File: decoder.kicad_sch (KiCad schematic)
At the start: 15 parts

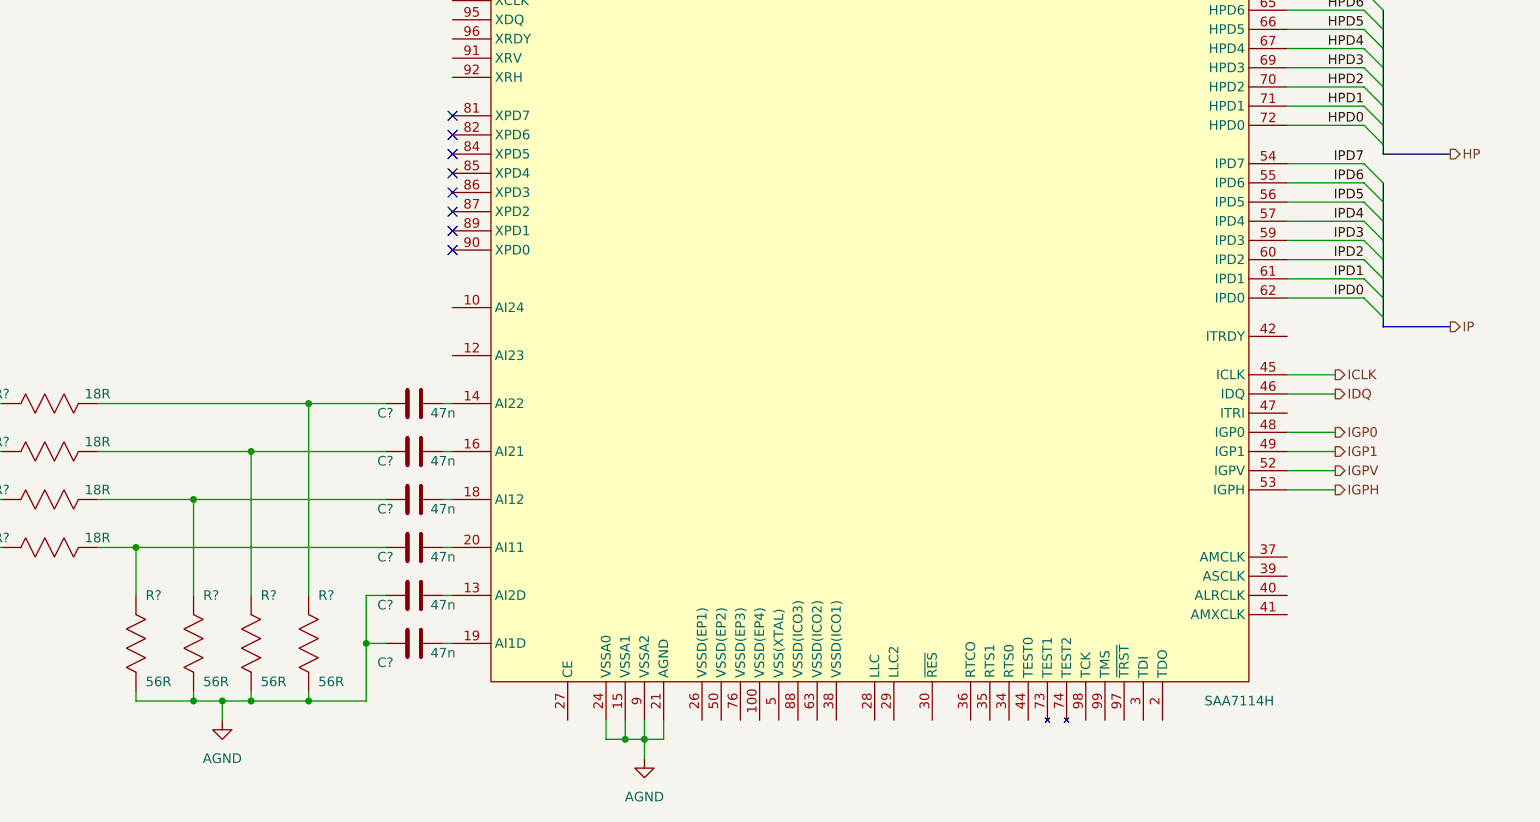
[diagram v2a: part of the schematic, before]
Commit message: added buses, title block info
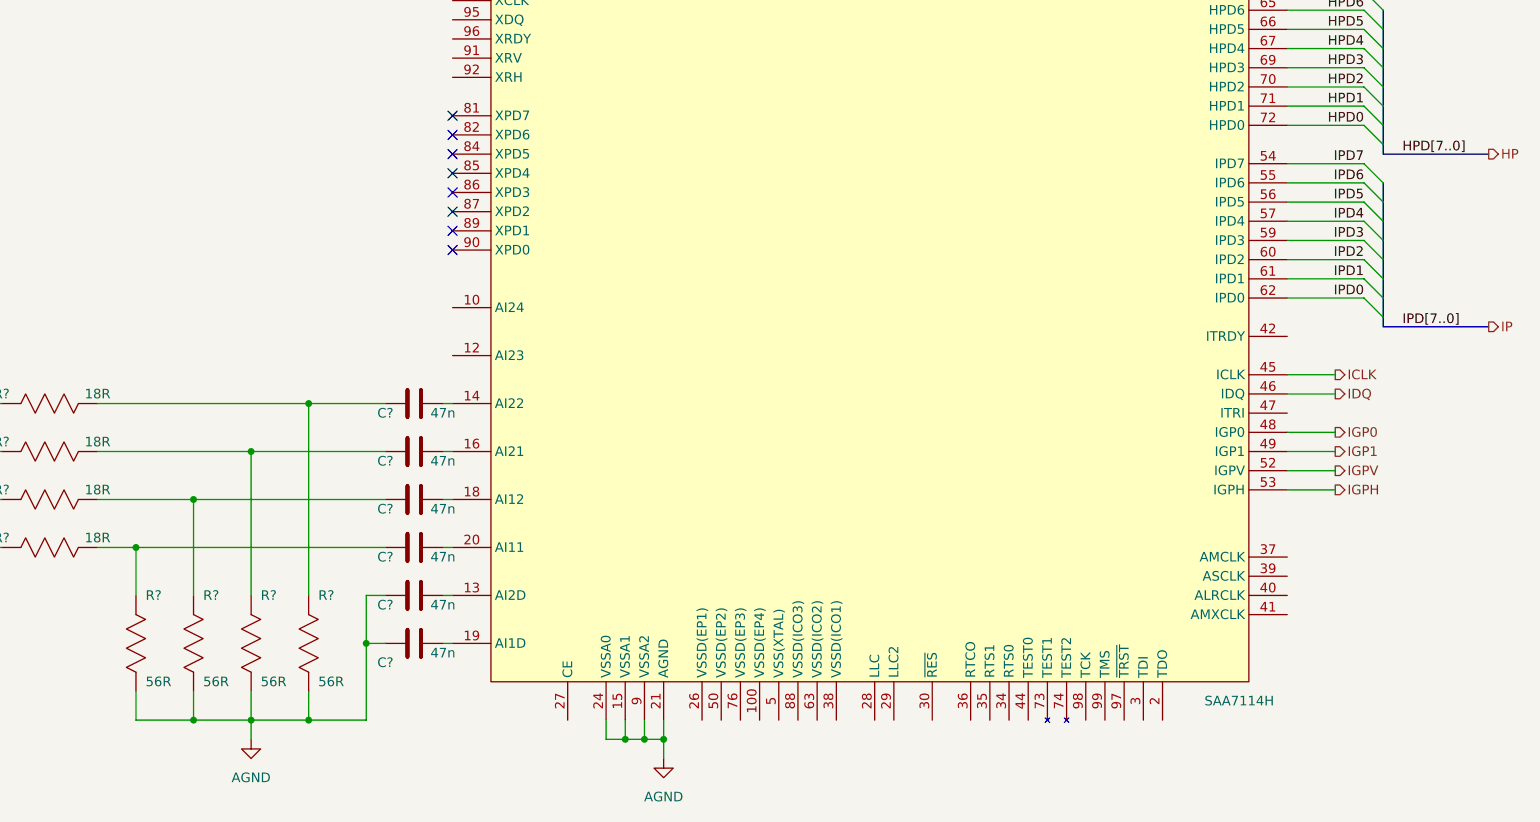
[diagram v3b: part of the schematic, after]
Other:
- title: (none) -> Time Base Corrector and Video Scaler
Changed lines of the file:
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@@
 (kicad_sch (version 20230121) (generator eeschema)
   (paper "A4")
+  (title_block
+    (title "Time Base Corrector and Video Scaler")
+    (date "2024-01-15")
+    (rev "1")
+  )
   (junction (at 71.12 121.92) (diameter 0) (color 0 0 0 0)
   )
-  (junction (at 78.74 148.59) (diameter 0) (color 0 0 0 0)
-  )
-  (junction (at 74.93 148.59) (diameter 0) (color 0 0 0 0)
+  (junction (at 78.74 151.13) (diameter 0) (color 0 0 0 0)
   )
   (junction (at 93.98 140.97) (diameter 0) (color 0 0 0 0)
@@
   (junction (at 63.5 128.27) (diameter 0) (color 0 0 0 0)
   )
+  (junction (at 133.35 153.67) (diameter 0) (color 0 0 0 0)
+  )
   (junction (at 130.81 153.67) (diameter 0) (color 0 0 0 0)
   )
-  (junction (at 71.12 148.59) (diameter 0) (color 0 0 0 0)
-  )
-  (junction (at 86.36 148.59) (diameter 0) (color 0 0 0 0)
+  (junction (at 71.12 151.13) (diameter 0) (color 0 0 0 0)
+  )
+  (junction (at 86.36 151.13) (diameter 0) (color 0 0 0 0)
   )
   (junction (at 78.74 115.57) (diameter 0) (color 0 0 0 0)
@@
     (stroke (width 0) (type default))
   )
+  (bus (pts (xy 228.6 97.79) (xy 228.6 99.06))
+    (stroke (width 0) (type default))
+  )
   (bus (pts (xy 228.6 95.25) (xy 228.6 97.79))
     (stroke (width 0) (type default))
@@
     (stroke (width 0) (type default))
   )
-  (wire (pts (xy 93.98 140.97) (xy 93.98 148.59))
+  (wire (pts (xy 93.98 140.97) (xy 93.98 151.13))
     (stroke (width 0) (type default))
   )
@@
     (stroke (width 0) (type default))
   )
-  (bus (pts (xy 228.6 76.2) (xy 237.49 76.2))
+  (bus (pts (xy 228.6 76.2) (xy 242.57 76.2))
     (stroke (width 0) (type default))
   )
@@
     (stroke (width 0) (type default))
   )
-  (wire (pts (xy 74.93 148.59) (xy 74.93 151.13))
+  (wire (pts (xy 78.74 151.13) (xy 78.74 153.67))
     (stroke (width 0) (type default))
   )
@@
     (stroke (width 0) (type default))
   )
-  (wire (pts (xy 71.12 148.59) (xy 74.93 148.59))
-    (stroke (width 0) (type default))
-  )
   (bus (pts (xy 228.6 57.15) (xy 228.6 59.69))
     (stroke (width 0) (type default))
@@
     (stroke (width 0) (type default))
   )
-  (wire (pts (xy 86.36 147.32) (xy 86.36 148.59))
-    (stroke (width 0) (type default))
-  )
-  (wire (pts (xy 78.74 148.59) (xy 86.36 148.59))
+  (wire (pts (xy 71.12 151.13) (xy 78.74 151.13))
+    (stroke (width 0) (type default))
+  )
+  (wire (pts (xy 86.36 147.32) (xy 86.36 151.13))
+    (stroke (width 0) (type default))
+  )
+  (wire (pts (xy 78.74 151.13) (xy 86.36 151.13))
     (stroke (width 0) (type default))
   )
@@
     (stroke (width 0) (type default))
   )
-  (wire (pts (xy 78.74 148.59) (xy 74.93 148.59))
-    (stroke (width 0) (type default))
-  )
   (bus (pts (xy 228.6 92.71) (xy 228.6 95.25))
     (stroke (width 0) (type default))
   )
-  (bus (pts (xy 228.6 99.06) (xy 237.49 99.06))
-    (stroke (width 0) (type default))
-  )
   (wire (pts (xy 215.9 105.41) (xy 222.25 105.41))
     (stroke (width 0) (type default))
@@
     (stroke (width 0) (type default))
   )
+  (bus (pts (xy 228.6 99.06) (xy 242.57 99.06))
+    (stroke (width 0) (type default))
+  )
   (wire (pts (xy 78.74 115.57) (xy 78.74 134.62))
     (stroke (width 0) (type default))
@@
     (stroke (width 0) (type default))
   )
-  (wire (pts (xy 63.5 148.59) (xy 71.12 148.59))
+  (wire (pts (xy 63.5 151.13) (xy 71.12 151.13))
     (stroke (width 0) (type default))
   )
@@
     (stroke (width 0) (type default))
   )
-  (wire (pts (xy 71.12 147.32) (xy 71.12 148.59))
+  (wire (pts (xy 71.12 147.32) (xy 71.12 151.13))
     (stroke (width 0) (type default))
   )
@@
     (stroke (width 0) (type default))
   )
-  (wire (pts (xy 130.81 153.67) (xy 130.81 156.21))
+  (wire (pts (xy 133.35 153.67) (xy 133.35 156.21))
     (stroke (width 0) (type default))
   )
@@
     (stroke (width 0) (type default))
   )
+  (wire (pts (xy 215.9 95.25) (xy 226.06 95.25))
+    (stroke (width 0) (type default))
+  )
+  (wire (pts (xy 63.5 147.32) (xy 63.5 151.13))
+    (stroke (width 0) (type default))
+  )
   (bus (pts (xy 228.6 64.77) (xy 228.6 67.31))
     (stroke (width 0) (type default))
   )
-  (bus (pts (xy 228.6 97.79) (xy 228.6 99.06))
-    (stroke (width 0) (type default))
-  )
   (wire (pts (xy 104.14 109.22) (xy 105.41 109.22))
     (stroke (width 0) (type default))
@@
     (stroke (width 0) (type default))
   )
-  (wire (pts (xy 63.5 148.59) (xy 63.5 147.32))
-    (stroke (width 0) (type default))
-  )
   (wire (pts (xy 93.98 134.62) (xy 93.98 140.97))
     (stroke (width 0) (type default))
@@
     (stroke (width 0) (type default))
   )
-  (wire (pts (xy 93.98 148.59) (xy 86.36 148.59))
+  (wire (pts (xy 93.98 151.13) (xy 86.36 151.13))
     (stroke (width 0) (type default))
   )
@@
     (stroke (width 0) (type default))
   )
-  (wire (pts (xy 215.9 95.25) (xy 226.06 95.25))
-    (stroke (width 0) (type default))
-  )
   (wire (pts (xy 78.74 115.57) (xy 96.52 115.57))
     (stroke (width 0) (type default))
@@
     (stroke (width 0) (type default))
   )
-  (wire (pts (xy 78.74 147.32) (xy 78.74 148.59))
+  (wire (pts (xy 78.74 147.32) (xy 78.74 151.13))
     (stroke (width 0) (type default))
   )
@@
     (effects (font (size 1.27 1.27)) (justify right bottom))
   )
+  (label "HPD[7..0]" (at 231.14 76.2 0) (fields_autoplaced)
+    (effects (font (size 1.27 1.27)) (justify left bottom))
+  )
   (label "HPD2" (at 226.06 67.31 180) (fields_autoplaced)
     (effects (font (size 1.27 1.27)) (justify right bottom))
+  )
+  (label "IPD[7..0]" (at 231.14 99.06 0) (fields_autoplaced)
+    (effects (font (size 1.27 1.27)) (justify left bottom))
   )
   (label "IPD4" (at 226.06 85.09 180) (fields_autoplaced)
@@
     (effects (font (size 1.27 1.27)) (justify left))
   )
-  (hierarchical_label "IP" (shape output) (at 237.49 99.06 0) (fields_autoplaced)
+  (hierarchical_label "IP" (shape output) (at 242.57 99.06 0) (fields_autoplaced)
     (effects (font (size 1.27 1.27)) (justify left))
   )
@@
     (effects (font (size 1.27 1.27)) (justify right))
   )
-  (hierarchical_label "HP" (shape output) (at 237.49 76.2 0) (fields_autoplaced)
+  (hierarchical_label "HP" (shape output) (at 242.57 76.2 0) (fields_autoplaced)
     (effects (font (size 1.27 1.27)) (justify left))
   )
@@
     )
   )
-  (symbol (lib_id "tbc:AGND") (at 130.81 156.21 0) (unit 1)
+  (symbol (lib_id "tbc:AGND") (at 133.35 156.21 0) (unit 1)
     (in_bom yes) (on_board yes) (dnp no) (fields_autoplaced)
-    (property "Reference" "#PWR02" (at 130.81 162.56 0)
-      (effects (font (size 1.27 1.27)) hide)
-    )
-    (property "Value" "AGND" (at 130.81 161.29 0)
-      (effects (font (size 1.27 1.27)))
-    )
-    (property "Footprint" "" (at 130.81 156.21 0)
-      (effects (font (size 1.27 1.27)) hide)
-    )
-    (property "Datasheet" "" (at 130.81 156.21 0)
+    (property "Reference" "#PWR02" (at 133.35 162.56 0)
+      (effects (font (size 1.27 1.27)) hide)
+    )
+    (property "Value" "AGND" (at 133.35 161.29 0)
+      (effects (font (size 1.27 1.27)))
+    )
+    (property "Footprint" "" (at 133.35 156.21 0)
+      (effects (font (size 1.27 1.27)) hide)
+    )
+    (property "Datasheet" "" (at 133.35 156.21 0)
       (effects (font (size 1.27 1.27)) hide)
     )
@@
     )
   )
-  (symbol (lib_id "tbc:AGND") (at 74.93 151.13 0) (unit 1)
+  (symbol (lib_id "tbc:AGND") (at 78.74 153.67 0) (unit 1)
     (in_bom yes) (on_board yes) (dnp no) (fields_autoplaced)
-    (property "Reference" "#PWR01" (at 74.93 157.48 0)
-      (effects (font (size 1.27 1.27)) hide)
-    )
-    (property "Value" "AGND" (at 74.93 156.21 0)
-      (effects (font (size 1.27 1.27)))
-    )
-    (property "Footprint" "" (at 74.93 151.13 0)
-      (effects (font (size 1.27 1.27)) hide)
-    )
-    (property "Datasheet" "" (at 74.93 151.13 0)
-      (effects (font (size 1.27 1.27)) hide)
-    )
+    (property "Reference" "#PWR01" (at 78.74 160.02 0)
+      (effects (font (size 1.27 1.27)) hide)
+    )
+    (property "Value" "AGND" (at 78.74 158.75 0)
+      (effects (font (size 1.27 1.27)))
+    )
+    (property "Footprint" "" (at 78.74 153.67 0)
+      (effects (font (size 1.27 1.27)) hide)
+    )
+    (property "Datasheet" "" (at 78.74 153.67 0)
+      (effects (font (size 1.27 1.27)) hide)
+    )

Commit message: added frame memory symbol and updated schematic
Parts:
- C? (x6): MPN GCJ188R71E473KA01D -> (none)
- R? (x4): MPN RC0603FR-0718RL -> (none)
- R? (x4): MPN RC0603FR-0756RL -> (none)
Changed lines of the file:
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@@
-      (effects (font (size 1.27 1.27)) (justify left) hide)
-    )
-    (property "MPN" "GCJ188R71E473KA01D" (at 86.36 129.54 0) (show_name)
       (effects (font (size 1.27 1.27)) (justify left) hide)
     )
@@
     )
     (property "Datasheet" "https://www.yageo.com/upload/media/product/products/datasheet/rchip/PYu-RC_Group_51_RoHS_L_12.pdf" (at 35.56 134.62 0) (show_name)
-      (effects (font (size 1.27 1.27)) (justify left) hide)
-    )
-    (property "MPN" "RC0603FR-0718RL" (at 35.56 129.54 0) (show_name)
       (effects (font (size 1.27 1.27)) (justify left) hide)
     )
@@
       (effects (font (size 1.27 1.27)) (justify right))
     )
-    (property "Value" "56R" (at 64.77 146.05 90)
-      (effects (font (size 1.27 1.27)) (justify right))
+    (property "Value" "56R" (at 64.77 146.05 0)
+      (effects (font (size 1.27 1.27)))
     )
     (property "Footprint" "" (at 71.12 157.48 0)
@@
     )
     (property "Datasheet" "https://www.yageo.com/upload/media/product/products/datasheet/rchip/PYu-RC_Group_51_RoHS_L_12.pdf" (at 76.2 157.48 0) (show_name)
-      (effects (font (size 1.27 1.27)) (justify left) hide)
-    )
-    (property "MPN" "RC0603FR-0756RL" (at 71.12 157.48 0) (show_name)
       (effects (font (size 1.27 1.27)) (justify left) hide)
     )
@@
       (effects (font (size 1.27 1.27)) (justify right))
     )
-    (property "Value" "56R" (at 80.01 146.05 90)
-      (effects (font (size 1.27 1.27)) (justify right))
+    (property "Value" "56R" (at 80.01 146.05 0)
+      (effects (font (size 1.27 1.27)))
     )
     (property "Footprint" "" (at 86.36 157.48 0)
@@
     )
     (property "Datasheet" "https://www.yageo.com/upload/media/product/products/datasheet/rchip/PYu-RC_Group_51_RoHS_L_12.pdf" (at 91.44 157.48 0) (show_name)
-      (effects (font (size 1.27 1.27)) (justify left) hide)
-    )
-    (property "MPN" "RC0603FR-0756RL" (at 86.36 157.48 0) (show_name)
       (effects (font (size 1.27 1.27)) (justify left) hide)
     )
@@
       (effects (font (size 1.27 1.27)) (justify left) hide)
     )
-    (property "MPN" "GCJ188R71E473KA01D" (at 86.36 123.19 0) (show_name)
-      (effects (font (size 1.27 1.27)) (justify left) hide)
-    )
     (property "Mouser" "81-GCJ188R71E473KA1D" (at 86.36 125.73 0) (show_name)
       (effects (font (size 1.27 1.27)) (justify left) hide)
@@
     )
     (property "Datasheet" "https://au.mouser.com/datasheet/2/281/1/GCJ188R71E473KA01_02B-3140701.pdf" (at 86.36 140.97 0) (show_name)
-      (effects (font (size 1.27 1.27)) (justify left) hide)
-    )
-    (property "MPN" "GCJ188R71E473KA01D" (at 86.36 135.89 0) (show_name)
       (effects (font (size 1.27 1.27)) (justify left) hide)
     )
@@
       (effects (font (size 1.27 1.27)) (justify right))
     )
-    (property "Value" "56R" (at 72.39 146.05 90)
-      (effects (font (size 1.27 1.27)) (justify right))
+    (property "Value" "56R" (at 72.39 146.05 0)
+      (effects (font (size 1.27 1.27)))
     )
     (property "Footprint" "" (at 78.74 157.48 0)
@@
       (effects (font (size 1.27 1.27)) (justify left) hide)
     )
-    (property "MPN" "RC0603FR-0756RL" (at 78.74 157.48 0) (show_name)
-      (effects (font (size 1.27 1.27)) (justify left) hide)
-    )
     (property "Mouser" " 603-RC0603FR-0756RL " (at 81.28 157.48 0) (show_name)
       (effects (font (size 1.27 1.27)) (justify left) hide)
@@
     )
     (property "Datasheet" "https://www.yageo.com/upload/media/product/products/datasheet/rchip/PYu-RC_Group_51_RoHS_L_12.pdf" (at 35.56 121.92 0) (show_name)
-      (effects (font (size 1.27 1.27)) (justify left) hide)
-    )
-    (property "MPN" "RC0603FR-0718RL" (at 35.56 116.84 0) (show_name)
       (effects (font (size 1.27 1.27)) (justify left) hide)
     )
@@
       (effects (font (size 1.27 1.27)) (justify left) hide)
     )
-    (property "MPN" "GCJ188R71E473KA01D" (at 86.36 116.84 0) (show_name)
-      (effects (font (size 1.27 1.27)) (justify left) hide)
-    )
     (property "Mouser" "81-GCJ188R71E473KA1D" (at 86.36 119.38 0) (show_name)
       (effects (font (size 1.27 1.27)) (justify left) hide)
@@
       (effects (font (size 1.27 1.27)) (justify left) hide)
     )
-    (property "MPN" "RC0603FR-0718RL" (at 35.56 123.19 0) (show_name)
-      (effects (font (size 1.27 1.27)) (justify left) hide)
-    )
     (property "Mouser" "603-RC0603FR-0718RL" (at 35.56 125.73 0) (show_name)
       (effects (font (size 1.27 1.27)) (justify left) hide)
@@
       (effects (font (size 1.27 1.27)) (justify left) hide)
     )
-    (property "MPN" "GCJ188R71E473KA01D" (at 86.36 142.24 0) (show_name)
-      (effects (font (size 1.27 1.27)) (justify left) hide)
-    )
     (property "Mouser" "81-GCJ188R71E473KA1D" (at 86.36 144.78 0) (show_name)
       (effects (font (size 1.27 1.27)) (justify left) hide)
@@
     )
     (property "Datasheet" "https://au.mouser.com/datasheet/2/281/1/GCJ188R71E473KA01_02B-3140701.pdf" (at 86.36 153.67 0) (show_name)
-      (effects (font (size 1.27 1.27)) (justify left) hide)
-    )
-    (property "MPN" "GCJ188R71E473KA01D" (at 86.36 148.59 0) (show_name)
       (effects (font (size 1.27 1.27)) (justify left) hide)
     )
@@
       (effects (font (size 1.27 1.27)) (justify right))
     )
-    (property "Value" "56R" (at 87.63 146.05 90)
-      (effects (font (size 1.27 1.27)) (justify right))
+    (property "Value" "56R" (at 87.63 146.05 0)
+      (effects (font (size 1.27 1.27)))
     )
     (property "Footprint" "" (at 93.98 157.48 0)
@@
       (effects (font (size 1.27 1.27)) (justify left) hide)
     )
-    (property "MPN" "RC0603FR-0756RL" (at 93.98 157.48 0) (show_name)
-      (effects (font (size 1.27 1.27)) (justify left) hide)
-    )
     (property "Mouser" " 603-RC0603FR-0756RL " (at 96.52 157.48 0) (show_name)
       (effects (font (size 1.27 1.27)) (justify left) hide)
@@
       (effects (font (size 1.27 1.27)) (justify left) hide)
     )
-    (property "MPN" "RC0603FR-0718RL" (at 35.56 135.89 0) (show_name)
-      (effects (font (size 1.27 1.27)) (justify left) hide)
-    )

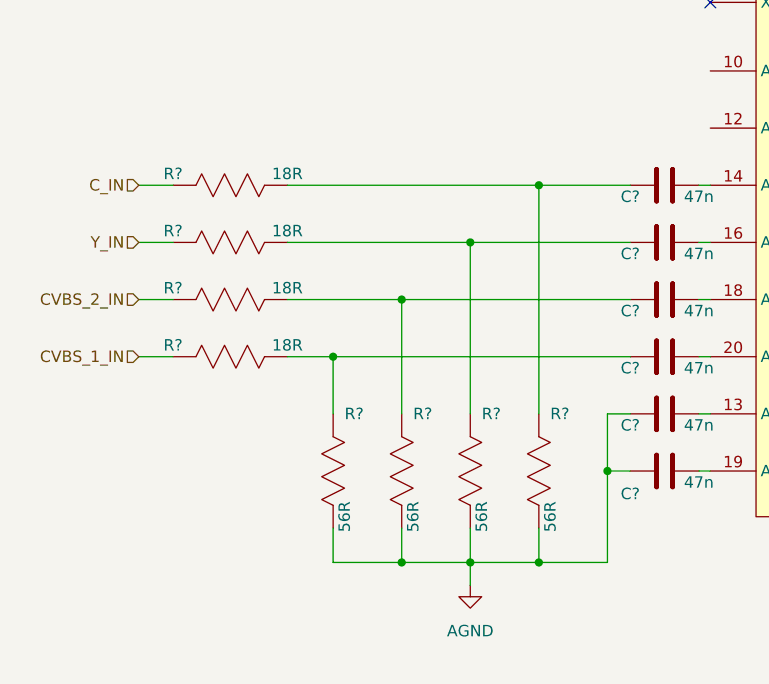
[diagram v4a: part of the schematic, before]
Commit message: continued on schematic, added power sheet
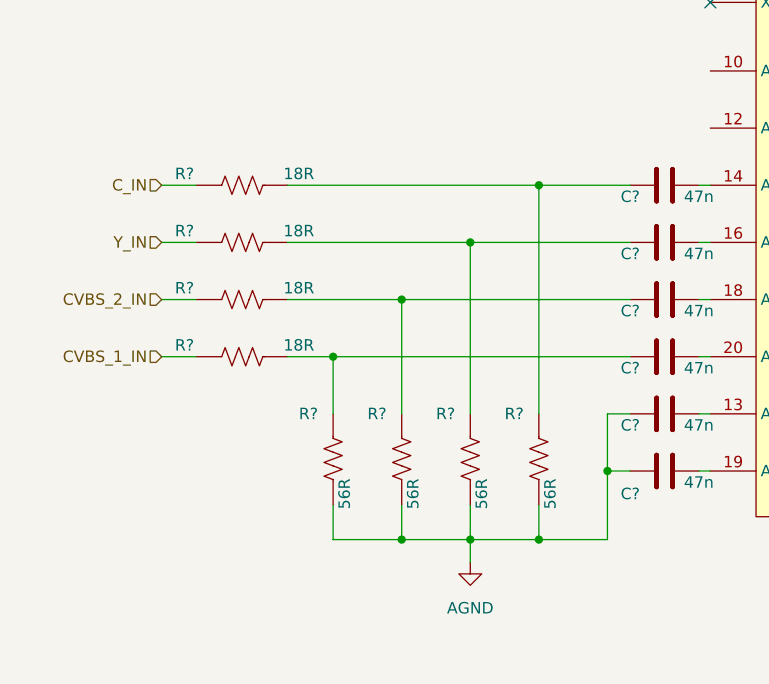
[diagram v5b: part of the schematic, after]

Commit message: updates to power, ferrites etc
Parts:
- added C?: 22u|25V, symbol tbc:GRM32ER71E226KE15L
- added C? (x13): 100n, symbol tbc:GCJ188R71H104KA12D
- added L?: 10uH, symbol tbc:DFE201610E-100M=P2
- R? (x4): value 18R -> 18
- R? (x4): value 56R -> 56
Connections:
- net AGND is gone; now on net GND: C?.1, C?.1, R?.1, R?.1, R?.1, R?.1, U?.15 (VSSA1), U?.21 (AGND), U?.24 (VSSA0), U?.9 (VSSA2)
- net +3V3: now reaches U?.1 (VDDD(EP1))
- net +3V3: now also U?.25 (VDDD(EP2)), U?.33 (VDDD(ICO1)), U?.43 (VDDD(ICO2)), U?.51 (VDDD(EP3)), U?.58 (VDDD(ICO3)), U?.68 (VDDD(ICO4)), U?.75 (VDDD(EP4)), U?.83 (VDDD(ICO5)), U?.93 (VDDD(ICO6)), C?.2, C?.2, C?.2, C?.2, C?.2, C?.2, C?.2, C?.2, C?.2, C?.2, L?.1
- net GND: now reaches U?.100 (VSSD(EP4))
- net GND: now also U?.26 (VSSD(EP1)), U?.38 (VSSD(ICO1)), U?.5 (VSS(XTAL)), U?.50 (VSSD(EP2)), U?.63 (VSSD(ICO2)), U?.76 (VSSD(EP3)), U?.88 (VSSD(ICO3)), C?.1, C?.1, C?.1, C?.1, C?.1, C?.1, C?.1, C?.1, C?.1, C?.1, C?.1, C?.1, C?.1, C?.1
- net +3V3A: now reaches U?.11 (VDDA2)
- net +3V3A: now also U?.17 (VDDA1), U?.23 (VDDA0), C?.2, C?.2, C?.2, C?.2, L?.2
